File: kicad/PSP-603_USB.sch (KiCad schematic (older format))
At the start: 39 parts, among them J1 10118193-0001LF, J2 826947-4, J3 5019, M1 9575, M2 9575, U1 93LC56BT-I/OT, U2 FT232HL-Reel, U3 SN74LV1T34DBVR, X1 ABM8G-12.000MHZ-18-D2Y-T

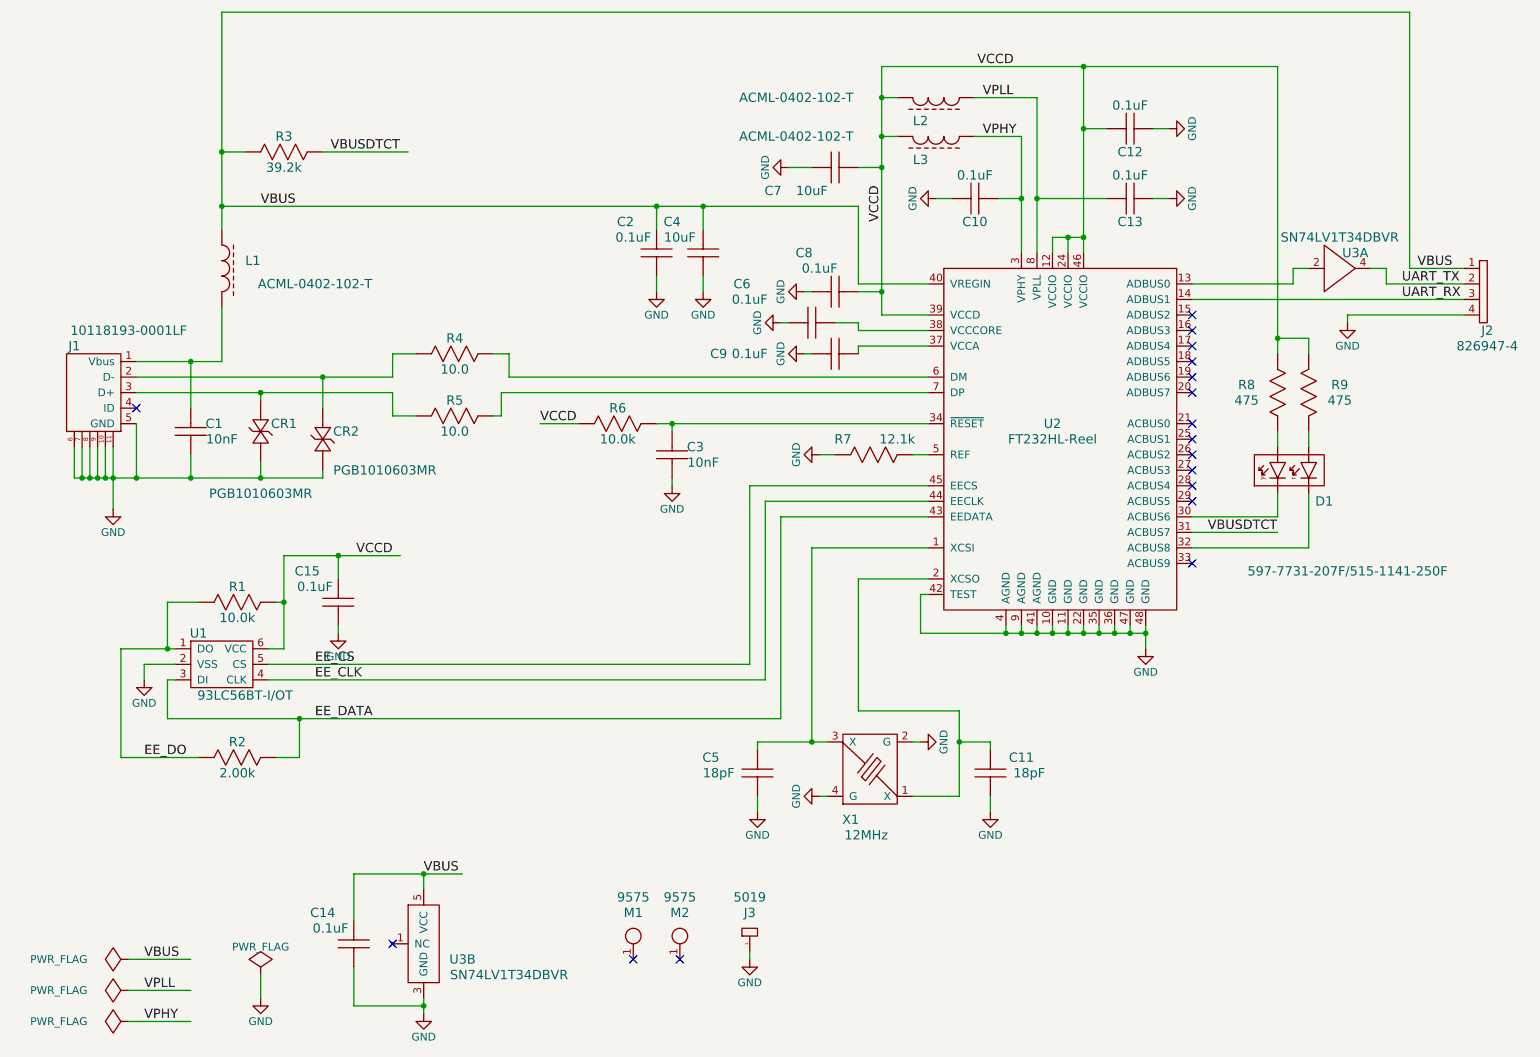
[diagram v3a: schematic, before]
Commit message: Switched to FT232R
Signed-off-by: Chris Stook <chris@chrisstook.com>
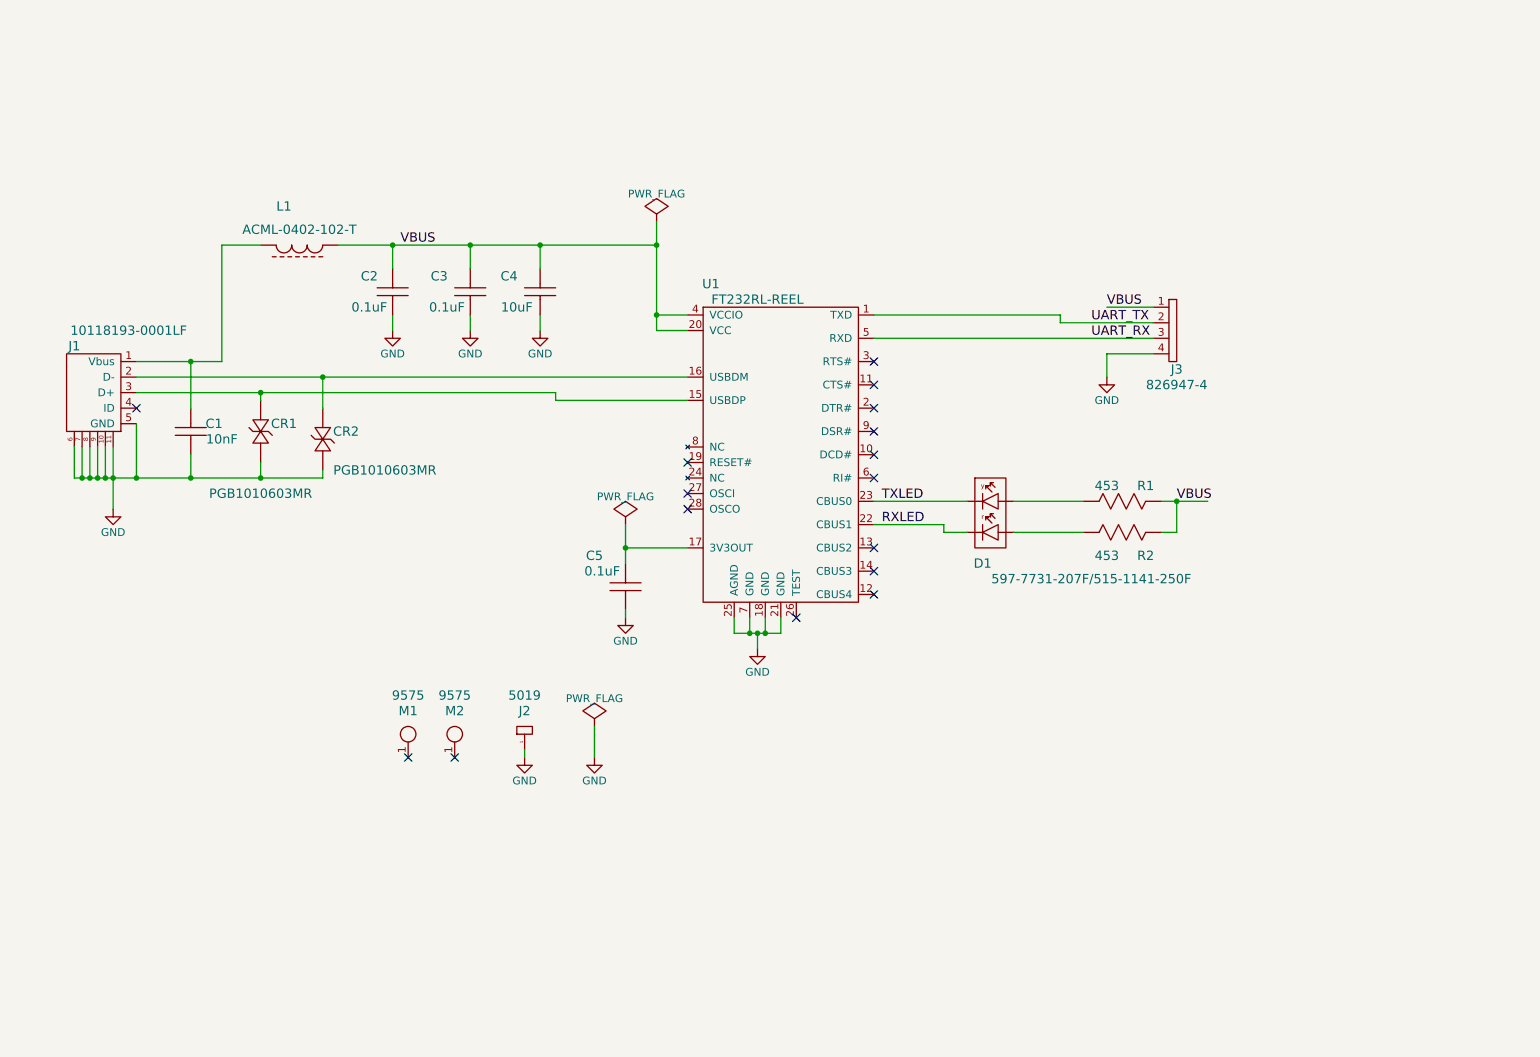
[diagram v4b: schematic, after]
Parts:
- removed C10, C12, C13, C14, C15, C6, C8, C9: C1005X7R1H104K050BB, Standard_Footprints:C0402, symbol C1005X7R1H104K050BB
- removed C11, C5: 04025A180JAT2A, Standard_Footprints:C0402, symbol 04025A180JAT2A
- removed C3: C0603C103J2RACTU, Standard_Footprints:C0603, symbol C0603C103J2RACTU
- removed C7: EMK212BB7106MG-T, Standard_Footprints:C0805, symbol EMK212BB7106MG-T
- removed L2, L3: ACML-0402-102-T, Standard_Footprints:C0402, symbol ACML-0402-102-T
- removed R1, R6: ERJ3EKF1002V, Standard_Footprints:R0603, symbol ERJ3EKF1002V
- removed R2: ERJ3EKF2001V, Standard_Footprints:R0603, symbol ERJ3EKF2001V
- removed R3: ERJ3EKF3922V, Standard_Footprints:R0603, symbol ERJ3EKF3922V
- removed R4, R5: ERJ3EKF10R0V, Standard_Footprints:R0603, symbol ERJ3EKF10R0V
- removed R7: ERJ3EKF1212V, Standard_Footprints:R0603, symbol ERJ3EKF1212V
- removed R8, R9: ERJ6ENF4750V, Standard_Footprints:R0805, symbol ERJ6ENF4750V
- removed U1: 93LC56BT-I/OT, Standard_Footprints:TSOT-32-6, symbol 93LC56BT-I/OT
- removed U2: FT232HL-Reel, FTDI_Footprints:LQFP_48, symbol FT232HL-Reel
- removed U3: SN74LV1T34DBVR, Standard_Footprints:TSOT-23-5, symbol SN74LV1T34DBVR
- removed X1: ABM8G-12.000MHZ-18-D2Y-T, Abracon_Footprints:ABM8G, symbol ABM8G-12.000MHZ-18-D2Y-T
- added C3, C5: C1005X7R1H104K050BB, Standard_Footprints:C0402, symbol C1005X7R1H104K050BB
- added R1, R2: CRCW0805453RFKEA, Standard_Footprints:R0805, symbol CRCW0805453RFKEA
- added U1: FT232RL-REEL, FTDI_Footprints:SSOP-28, symbol FT232RL-REEL
- renumbered J3 to J2, J2 to J3
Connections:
- net labels added: RXLED, TXLED
- net labels removed: EE_CLK, EE_CS, EE_DATA, EE_DO, VBUSDTCT, VCCD, VPHY, VPLL
- wire segments 162 -> 58
- no-connect marks 17 -> 16
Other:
- moved on the sheet: D1, J2, J3, L1, M1, M2

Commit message: redo layout Signed-off-by: Chris Stook <chris@chrisstook.com>
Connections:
- net GND: now also M1.1, M2.1; no longer J1.10, J1.11, J1.6, J1.7, J1.8, J1.9
- net D+: now reaches CR1.1, J1.3 (D+), U1.15 (USBDP)
- net RXLEDANNODE: now reaches D1.2 (RA), R2.1
- net TXLEDANNODE: now reaches D1.4 (YA), R1.1
- net D-: now reaches CR2.1, J1.2 (D-), U1.16 (USBDM)
- net +5v: now reaches C1.2, J1.1 (Vbus), L1.2
- net 3r3v: now reaches C5.2, U1.17 (3V3OUT)
- new net Shield: J1.10, J1.11, J1.6, J1.7, J1.8, J1.9
- no-connect marks 16 -> 14
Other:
- moved on the sheet: R1, R2
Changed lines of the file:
@@
 L GND #PWR01
 U 1 1 56C7C162
-P 1400 4350
-F 0 "#PWR01" H 1400 4100 50  0001 C CNN
-F 1 "GND" H 1400 4200 50  0000 C CNN
-F 2 "" H 1400 4350 50  0000 C CNN
-F 3 "" H 1400 4350 50  0000 C CNN
-	1    1400 4350
+P 1550 4250
+F 0 "#PWR01" H 1550 4000 50  0001 C CNN
+F 1 "GND" H 1550 4100 50  0000 C CNN
+F 2 "" H 1550 4250 50  0000 C CNN
+F 3 "" H 1550 4250 50  0000 C CNN
+	1    1550 4250
 	1    0    0    -1
 $EndComp
 Wire Wire Line
 	1150 3950 1150 4150
-Wire Wire Line
-	1150 4150 2750 4150
 Wire Wire Line
 	1200 4150 1200 3950
@@
 	1350 4150 1350 3950
 Connection ~ 1300 4150
-Wire Wire Line
-	1400 3950 1400 4350
 Connection ~ 1350 4150
-Connection ~ 1400 4150
-Wire Wire Line
-	1550 4150 1550 3800
+Wire Wire Line
+	1550 3800 1550 4250
 $Comp
 L PGB1010603MR CR2
@@
 Wire Wire Line
 	2350 4150 2350 4050
-Connection ~ 1550 4150
 Connection ~ 2350 4150
 Wire Wire Line
@@
 	0    -1   -1   0
 $EndComp
-NoConn ~ 3300 5950
-NoConn ~ 3600 5950
 $Comp
 L 10118193-0001LF J1
@@
 	6750 4500 6900 4500
 Wire Wire Line
-	7200 4300 7650 4300
-Wire Wire Line
-	7200 4500 7650 4500
-Wire Wire Line
-	8150 4500 8250 4500
-Wire Wire Line
-	8150 4300 8450 4300
-Text Label 8250 4300 0    60   ~ 0
+	7200 4300 7950 4300
+Wire Wire Line
+	7200 4500 7950 4500
+Wire Wire Line
+	8450 4500 8550 4500
+Wire Wire Line
+	8450 4300 8750 4300
+Text Label 8550 4300 0    60   ~ 0
 VBUS
 Wire Wire Line
-	8250 4500 8250 4300
-Connection ~ 8250 4300
+	8550 4500 8550 4300
+Connection ~ 8550 4300
 Wire Wire Line
 	6300 3100 7500 3100
@@
 L CRCW0805453RFKEA R1
 U 1 1 56F64E6A
-P 7900 4300
-F 0 "R1" H 8050 4400 60  0000 C CNN
-F 1 "CRCW0805453RFKEA" H 8000 3900 60  0001 C CNN
-F 2 "Standard_Footprints:R0805" H 8000 3800 60  0001 C CNN
-F 3 "C:/Users/Chris/VendorData/Vishay/dcrcwe3.pdf" H 8050 3500 60  0001 C CNN
-F 4 " 453 " H 7800 4400 60  0000 C CNN "Resistance"
-F 5 "Vishay" H 7900 3700 60  0001 C CNN "mfg"
-F 6 "CRCW0805453RFKEA" H 8050 4000 60  0001 C CNN "mfg part number"
-F 7 "1%" H 7750 4100 60  0001 C CNN "Tolerance"
-F 8 "0.125W" H 8000 4100 60  0001 C CNN "Power"
-F 9 "Thick Film" H 7900 3600 60  0001 C CNN "Composition"
-	1    7900 4300
+P 8200 4300
+F 0 "R1" H 8350 4400 60  0000 C CNN
+F 1 "CRCW0805453RFKEA" H 8300 3900 60  0001 C CNN
+F 2 "Standard_Footprints:R0805" H 8300 3800 60  0001 C CNN
+F 3 "C:/Users/Chris/VendorData/Vishay/dcrcwe3.pdf" H 8350 3500 60  0001 C CNN
+F 4 " 453 " H 8100 4400 60  0000 C CNN "Resistance"
+F 5 "Vishay" H 8200 3700 60  0001 C CNN "mfg"
+F 6 "CRCW0805453RFKEA" H 8350 4000 60  0001 C CNN "mfg part number"
+F 7 "1%" H 8050 4100 60  0001 C CNN "Tolerance"
+F 8 "0.125W" H 8300 4100 60  0001 C CNN "Power"
+F 9 "Thick Film" H 8200 3600 60  0001 C CNN "Composition"
+	1    8200 4300
 	1    0    0    -1
 $EndComp
@@
 L CRCW0805453RFKEA R2
 U 1 1 56F6517F
-P 7900 4500
-F 0 "R2" H 8050 4350 60  0000 C CNN
-F 1 "CRCW0805453RFKEA" H 8000 4100 60  0001 C CNN
-F 2 "Standard_Footprints:R0805" H 8000 4000 60  0001 C CNN
-F 3 "C:/Users/Chris/VendorData/Vishay/dcrcwe3.pdf" H 8050 3700 60  0001 C CNN
-F 4 " 453 " H 7800 4350 60  0000 C CNN "Resistance"
-F 5 "Vishay" H 7900 3900 60  0001 C CNN "mfg"
-F 6 "CRCW0805453RFKEA" H 8050 4200 60  0001 C CNN "mfg part number"
-F 7 "1%" H 7750 4300 60  0001 C CNN "Tolerance"
-F 8 "0.125W" H 8000 4300 60  0001 C CNN "Power"
-F 9 "Thick Film" H 7900 3800 60  0001 C CNN "Composition"
-	1    7900 4500
-	1    0    0    -1
-$EndComp
+P 8200 4500
+F 0 "R2" H 8350 4350 60  0000 C CNN
+F 1 "CRCW0805453RFKEA" H 8300 4100 60  0001 C CNN
+F 2 "Standard_Footprints:R0805" H 8300 4000 60  0001 C CNN
+F 3 "C:/Users/Chris/VendorData/Vishay/dcrcwe3.pdf" H 8350 3700 60  0001 C CNN
+F 4 " 453 " H 8100 4350 60  0000 C CNN "Resistance"
+F 5 "Vishay" H 8200 3900 60  0001 C CNN "mfg"
+F 6 "CRCW0805453RFKEA" H 8350 4200 60  0001 C CNN "mfg part number"
+F 7 "1%" H 8050 4300 60  0001 C CNN "Tolerance"
+F 8 "0.125W" H 8300 4300 60  0001 C CNN "Power"
+F 9 "Thick Film" H 8200 3800 60  0001 C CNN "Composition"
+	1    8200 4500
+	1    0    0    -1
+$EndComp
+$Comp
+L GND #PWR013
+U 1 1 56F6A57A
+P 3600 6050
+F 0 "#PWR013" H 3600 5800 50  0001 C CNN
+F 1 "GND" H 3600 5900 50  0000 C CNN
+F 2 "" H 3600 6050 50  0000 C CNN
+F 3 "" H 3600 6050 50  0000 C CNN
+	1    3600 6050
+	1    0    0    -1
+$EndComp
+$Comp
+L GND #PWR014
+U 1 1 56F6A5B8
+P 3300 6050
+F 0 "#PWR014" H 3300 5800 50  0001 C CNN
+F 1 "GND" H 3300 5900 50  0000 C CNN
+F 2 "" H 3300 6050 50  0000 C CNN
+F 3 "" H 3300 6050 50  0000 C CNN
+	1    3300 6050
+	1    0    0    -1
+$EndComp
+Wire Wire Line
+	3600 5950 3600 6050
+Wire Wire Line
+	3300 5950 3300 6050
+Wire Wire Line
+	1400 3950 1400 4350
+Wire Wire Line
+	1150 4150 1400 4150
+Wire Wire Line
+	1550 4150 2750 4150
+Connection ~ 1550 4150
+Text Label 2100 3150 1    60   ~ 0
++5v
+Text Label 1600 3500 0    60   ~ 0
+D-
+Text Label 1600 3600 0    60   ~ 0
+D+
+Wire Wire Line
+	1400 4350 750  4350
+Connection ~ 1400 4150
+Text Label 750  4350 0    60   ~ 0
+Shield
+Text Label 4750 4600 0    60   ~ 0
+3r3v
+Text Label 7250 4300 0    60   ~ 0
+TXLEDANNODE
+Text Label 7250 4500 0    60   ~ 0
+RXLEDANNODE
 $EndSCHEMATC

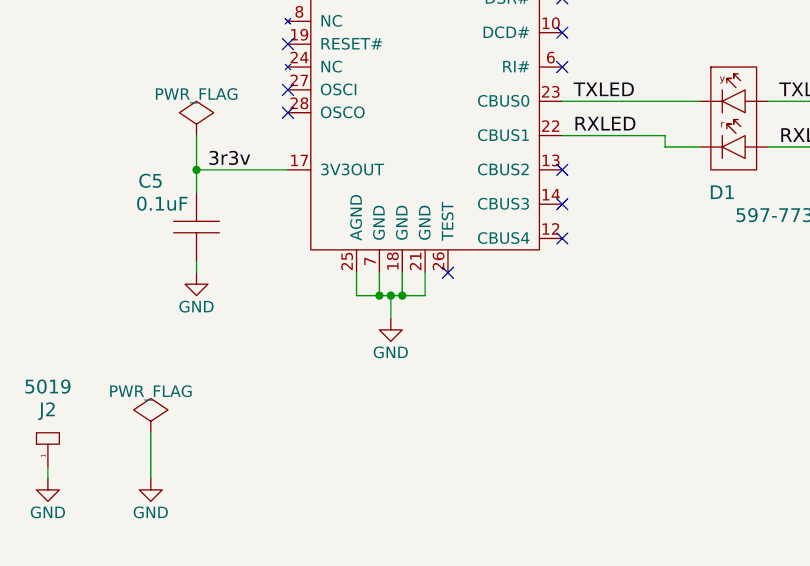
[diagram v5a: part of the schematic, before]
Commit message: tied test pin to gnd.
Signed-off-by: Chris Stook <chris@chrisstook.com>
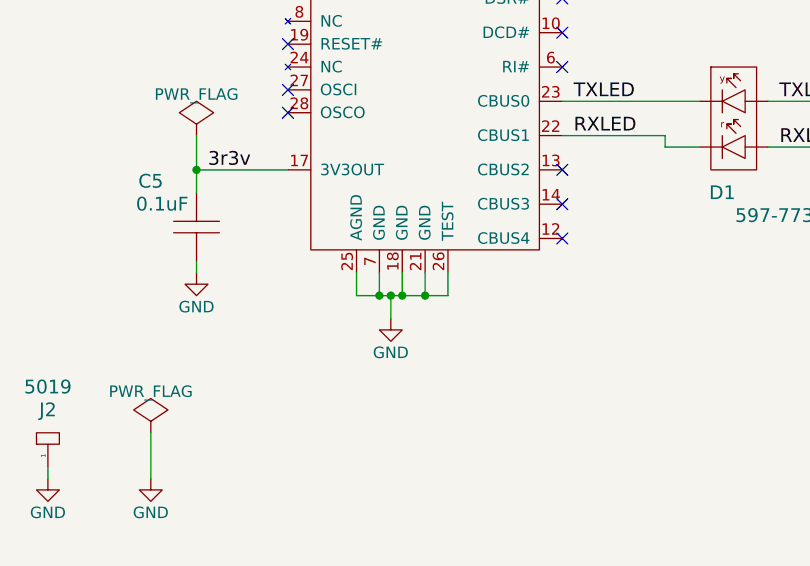
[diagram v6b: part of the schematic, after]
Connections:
- net GND: now also U1.26 (TEST)
- no-connect marks 14 -> 13
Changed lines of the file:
@@
 	5400 5050 5400 5150
 Wire Wire Line
-	5400 5150 5700 5150
+	5400 5150 5800 5150
 Wire Wire Line
 	5700 5150 5700 5050
@@
 NoConn ~ 6300 4750
 NoConn ~ 6300 4900
-NoConn ~ 5800 5050
 $Comp
 L PWR_FLAG #FLG012
@@
 Text Label 7250 4500 0    60   ~ 0
 RXLEDANNODE
+Wire Wire Line
+	5800 5150 5800 5050
+Connection ~ 5700 5150
 $EndSCHEMATC
